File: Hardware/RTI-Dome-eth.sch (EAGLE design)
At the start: 87 parts, among them IC1 24AA128ST, IC3 FT232RL, IC4 REG1117, IC5 74LVC245, IC6 74ABT245, J1 POWERPOLE_POWER45A, U1 W5500, X13 PN61729-S, X9 J1011F21PNL

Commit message: Fix some componenent manufacturer reference
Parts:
- IC6: device rti:74LVC245 -> rti:74ABT245
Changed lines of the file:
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@@
 <part name="X6" library="con-ptr500" deviceset="AK500/6" device=""/>
 <part name="IC5" library="rti" deviceset="74*245" device="" technology="LVC"/>
-<part name="IC6" library="rti" deviceset="74*245" device="" technology="LVC" value="74ABT245"/>
+<part name="IC6" library="rti" deviceset="74*245" device="" technology="ABT" value="74ABT245"/>
 <part name="GND7" library="supply1" deviceset="GND" device=""/>
 <part name="R22" library="rti" deviceset="R-EU" device="'0805'" value="4.7K"/>

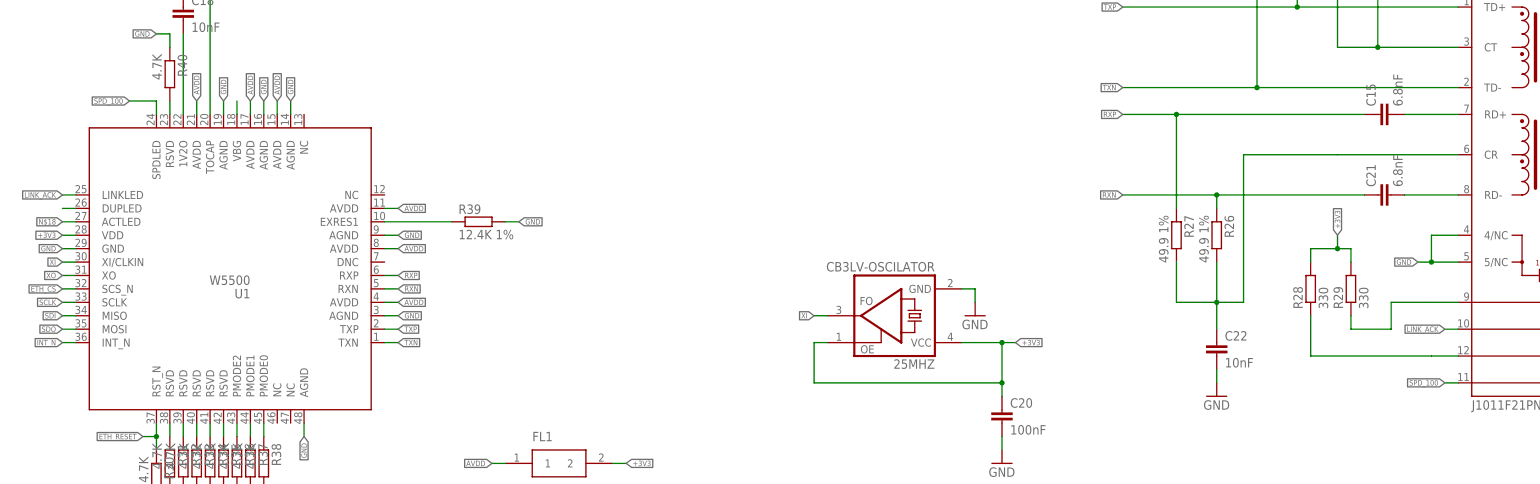
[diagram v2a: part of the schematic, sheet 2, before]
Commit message: Fix ethernet LED.
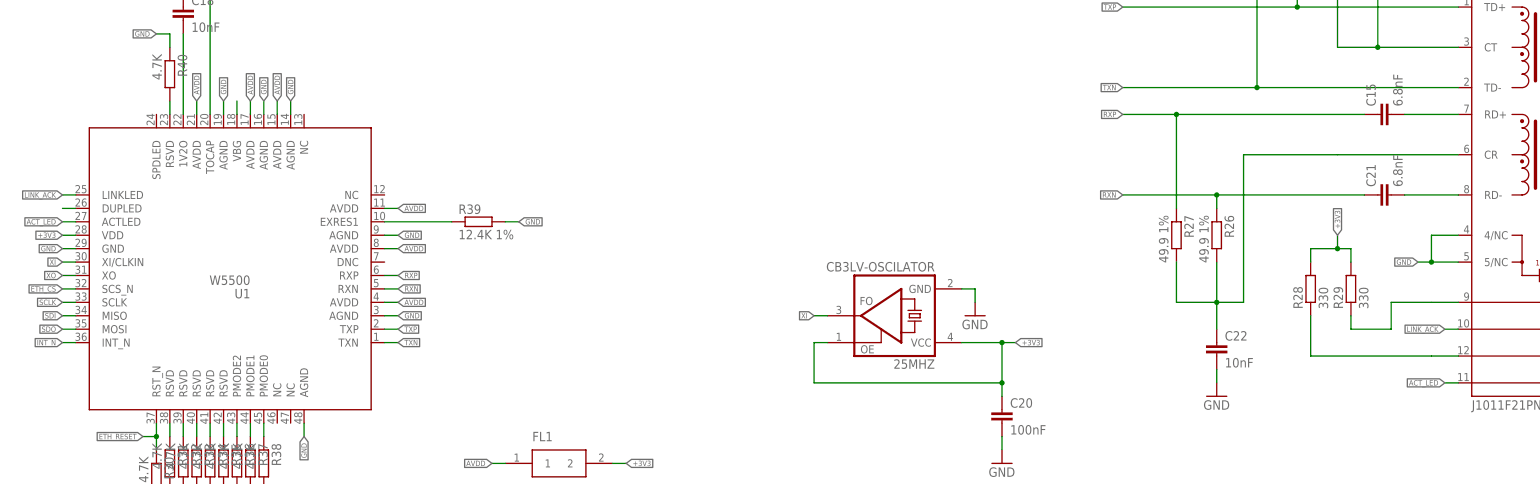
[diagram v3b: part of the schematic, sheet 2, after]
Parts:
- C25, C26: device rti:C-EU'1206' -> rti:C-EU'0805'
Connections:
- removed net N$18: U1.ACTLED
- removed net SPD_100: U1.SPDLED, X9.C-L
- new net ACT_LED: U1.ACTLED, X9.C-L
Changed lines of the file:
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@@
 <part name="+3V1" library="supply1" deviceset="+3V3" device=""/>
 <part name="P+13" library="supply1" deviceset="VCC" device=""/>
-<part name="C25" library="rti" deviceset="C-EU" device="'1206'" value="10uF"/>
-<part name="C26" library="rti" deviceset="C-EU" device="'1206'" value="10uF"/>
+<part name="C25" library="rti" deviceset="C-EU" device="'0805'" value="10uF"/>
+<part name="C26" library="rti" deviceset="C-EU" device="'0805'" value="10uF"/>
 <part name="GND20" library="supply1" deviceset="GND" device=""/>
 <part name="C15" library="rti" deviceset="C-EU" device="'0805'" value="6.8nF"/>
@@
 </segment>
 </net>
-<net name="SPD_100" class="0">
-<segment>
-<pinref part="X9" gate="G$1" pin="C-L"/>
-<wire x1="307.34" y1="149.86" x2="309.88" y2="149.86" width="0.1524" layer="91"/>
-<label x="307.34" y="149.86" size="1.016" layer="95" rot="R180" xref="yes"/>
-</segment>
-<segment>
-<pinref part="U1" gate="G$1" pin="SPDLED"/>
-<wire x1="63.5" y1="203.2" x2="63.5" y2="200.66" width="0.1524" layer="91"/>
-<wire x1="63.5" y1="203.2" x2="58.42" y2="203.2" width="0.1524" layer="91"/>
-<label x="58.42" y="203.2" size="1.016" layer="95" rot="R180" xref="yes"/>
-</segment>
-</net>
 <net name="LINK_ACK" class="0">
 <segment>
@@
 </segment>
 </net>
-<net name="N$18" class="0">
+<net name="ACT_LED" class="0">
 <segment>
 <pinref part="U1" gate="G$1" pin="ACTLED"/>
@@
 <label x="45.72" y="180.34" size="1.016" layer="95" rot="R180" xref="yes"/>
 </segment>
-</net>
+<segment>
+<pinref part="X9" gate="G$1" pin="C-L"/>
+<wire x1="307.34" y1="149.86" x2="309.88" y2="149.86" width="0.1524" layer="91"/>
+<label x="307.34" y="149.86" size="1.016" layer="95" rot="R180" xref="yes"/>
+</segment>
+</net>

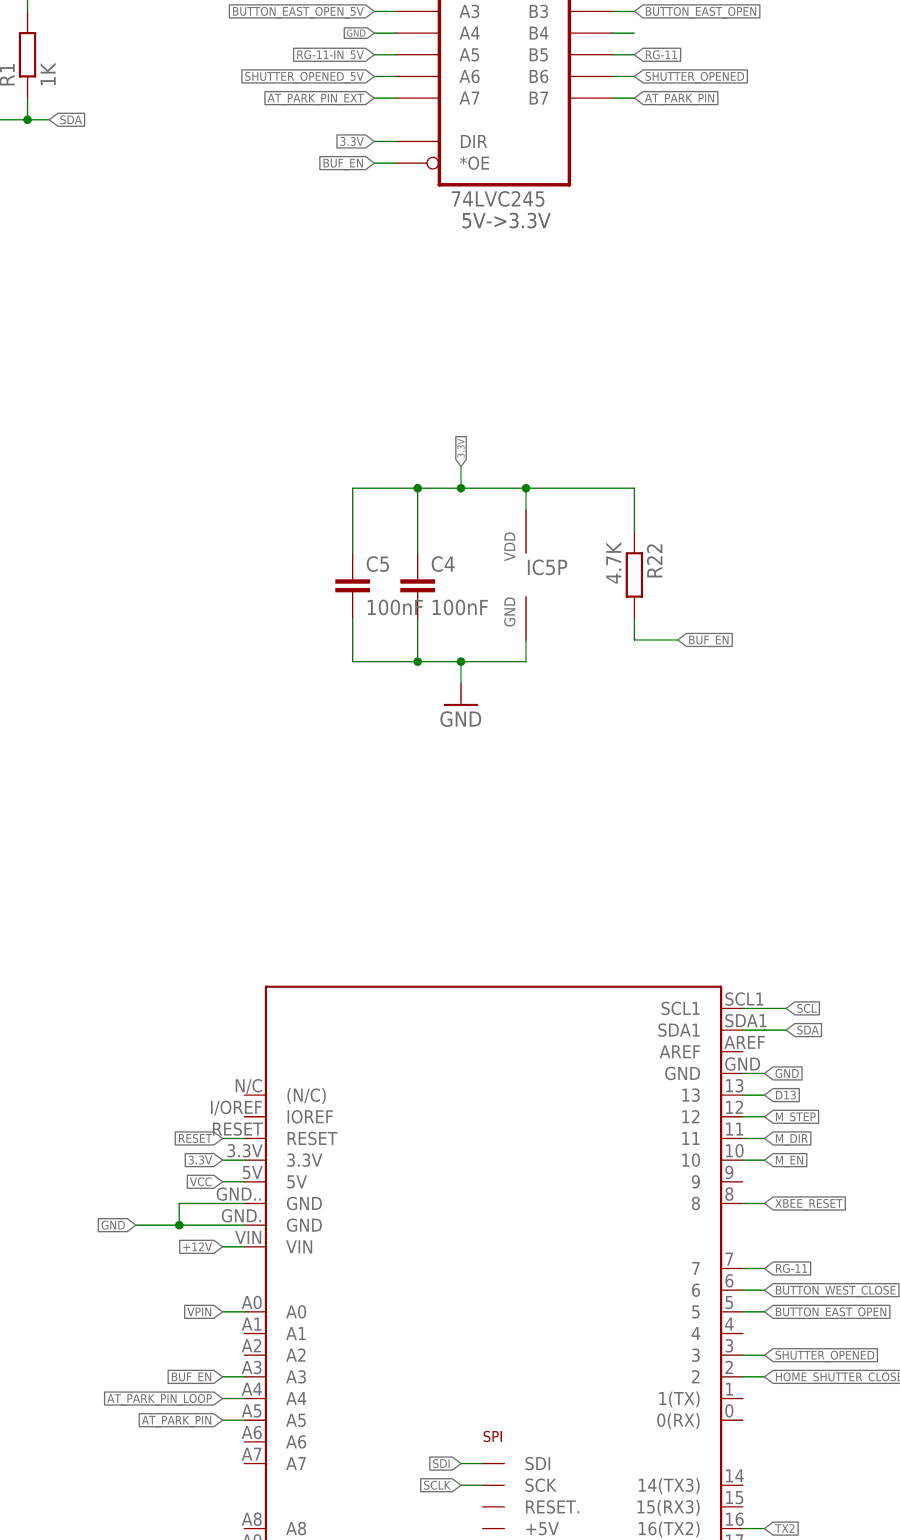
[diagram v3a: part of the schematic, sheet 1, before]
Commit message: Trace optimisation around the FTDI chip
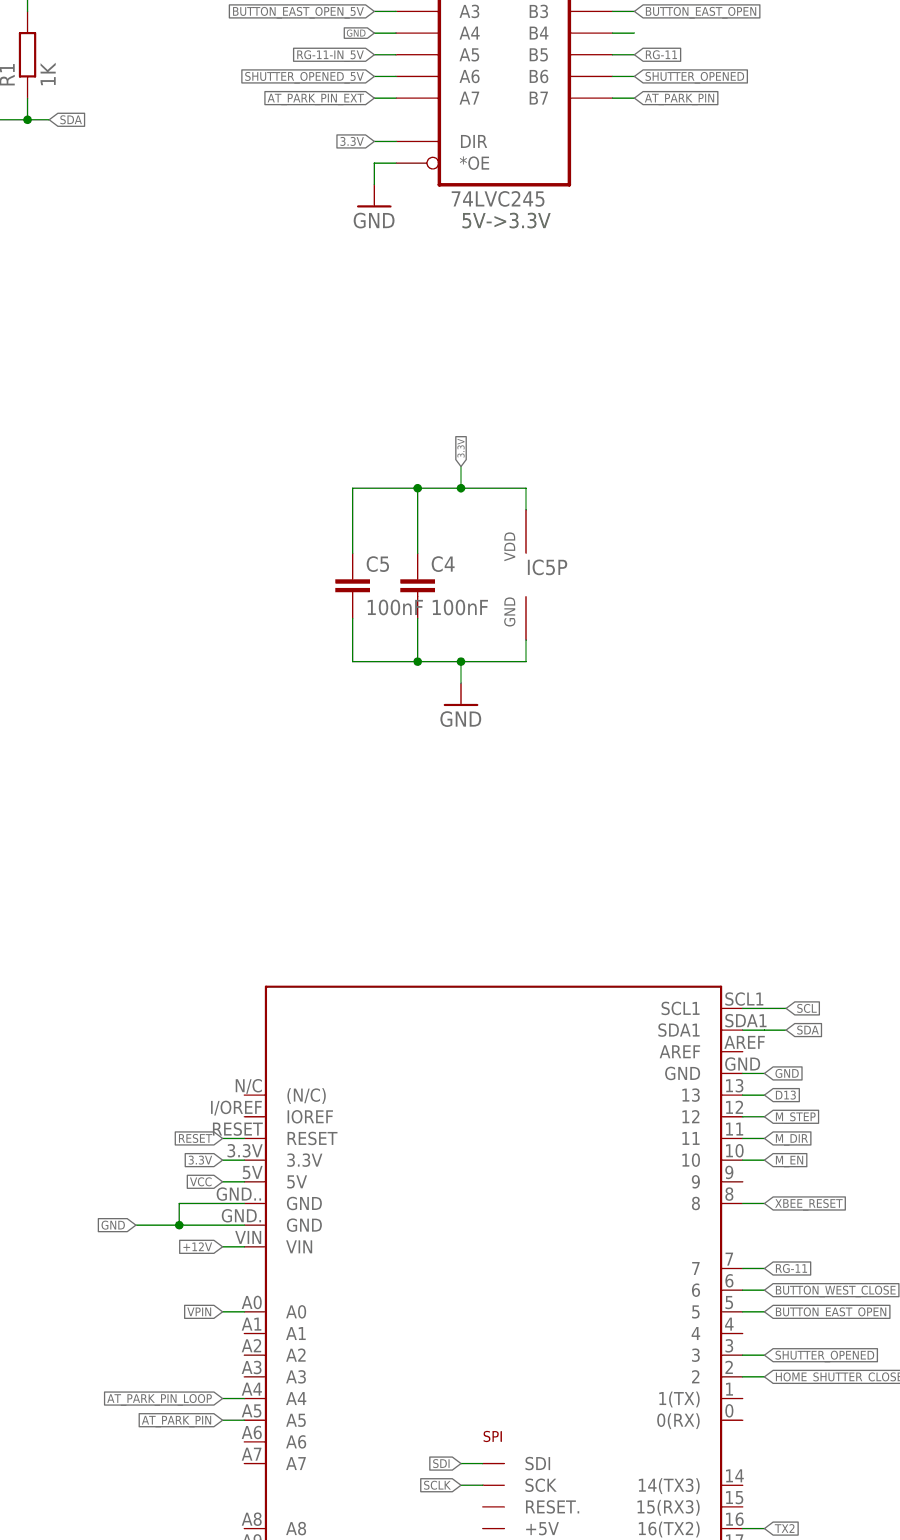
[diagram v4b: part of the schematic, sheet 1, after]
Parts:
- removed R22: 4.7K, rti:R-EU'0805'
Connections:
- removed net BUF_EN: IC5G$1.*OE, R22.2, U$1.A3
- net +12V: now also C25.1, IC4.VIN
- net 3.3V: no longer R22.1
- net GND: now also IC5G$1.*OE
- net VCC: no longer C25.1, IC4.VIN
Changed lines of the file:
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@@
 <part name="IC6" library="rti" deviceset="74*245" device="" technology="ABT" value="74ABT245"/>
 <part name="GND7" library="supply1" deviceset="GND" device=""/>
-<part name="R22" library="rti" deviceset="R-EU" device="'0805'" value="4.7K"/>
 <part name="U$1" library="arduino_shield" deviceset="ARDUINO_DUE_SHIELD_FULL" device=""/>
 <part name="GND9" library="supply1" deviceset="GND" device=""/>
@@
 <part name="IC4" library="burr-brown" deviceset="REG1117" device=""/>
 <part name="+3V1" library="supply1" deviceset="+3V3" device=""/>
-<part name="P+13" library="supply1" deviceset="VCC" device=""/>
 <part name="C25" library="rti" deviceset="C-EU" device="'0805'" value="10uF"/>
 <part name="C26" library="rti" deviceset="C-EU" device="'0805'" value="10uF"/>
@@
 <part name="GND19" library="supply1" deviceset="GND" device=""/>
 <part name="FRAME2" library="frames" deviceset="DINA3_L" device=""/>
+<part name="GND16" library="supply1" deviceset="GND" device=""/>
 </parts>
 <sheets>
@@
 <instance part="IC6" gate="P" x="203.2" y="180.34" rot="R270"/>
 <instance part="GND7" gate="1" x="187.96" y="226.06"/>
-<instance part="R22" gate="G$1" x="147.32" y="180.34" rot="R270"/>
 <instance part="U$1" gate="G$1" x="132.08" y="86.36"/>
 <instance part="GND9" gate="1" x="109.22" y="10.16"/>
@@
 <instance part="U$2" gate="G$1" x="53.34" y="63.5"/>
 <instance part="GND18" gate="1" x="38.1" y="55.88"/>
+<instance part="GND16" gate="1" x="116.84" y="223.52"/>
 </instances>
 <busses>
@@
 <pinref part="GND18" gate="1" pin="GND"/>
 </segment>
+<segment>
+<pinref part="IC5" gate="G$1" pin="*OE"/>
+<wire x1="119.38" y1="228.6" x2="116.84" y2="228.6" width="0.1524" layer="91"/>
+<wire x1="116.84" y1="228.6" x2="116.84" y2="226.06" width="0.1524" layer="91"/>
+<pinref part="GND16" gate="1" pin="GND"/>
+</segment>
 </net>
 <net name="+12V" class="1">
@@
 <junction x="121.92" y="190.5"/>
 <pinref part="IC5" gate="P" pin="VDD"/>
-<pinref part="R22" gate="G$1" pin="1"/>
-<wire x1="134.62" y1="190.5" x2="147.32" y2="190.5" width="0.1524" layer="91"/>
-<wire x1="147.32" y1="190.5" x2="147.32" y2="185.42" width="0.1524" layer="91"/>
-<junction x="134.62" y="190.5"/>
 </segment>
 <segment>
@@
 <wire x1="307.34" y1="160.02" x2="307.34" y2="157.48" width="0.1524" layer="91"/>
 <junction x="307.34" y="160.02"/>
-</segment>
-</net>
-<net name="BUF_EN" class="0">
-<segment>
-<pinref part="IC5" gate="G$1" pin="*OE"/>
-<wire x1="116.84" y1="228.6" x2="119.38" y2="228.6" width="0.1524" layer="91"/>
-<label x="116.84" y="228.6" size="1.016" layer="95" rot="R180" xref="yes"/>
-</segment>
-<segment>
-<pinref part="R22" gate="G$1" pin="2"/>
-<wire x1="152.4" y1="172.72" x2="147.32" y2="172.72" width="0.1524" layer="91"/>
-<wire x1="147.32" y1="172.72" x2="147.32" y2="175.26" width="0.1524" layer="91"/>
-<label x="152.4" y="172.72" size="1.016" layer="95" xref="yes"/>
-</segment>
-<segment>
-<wire x1="99.06" y1="86.36" x2="101.6" y2="86.36" width="0.1524" layer="91"/>
-<label x="99.06" y="86.36" size="1.016" layer="95" rot="R180" xref="yes"/>
-<pinref part="U$1" gate="G$1" pin="A3"/>
 </segment>
 </net>
@@
 <instance part="IC4" gate="G$1" x="58.42" y="27.94"/>
 <instance part="+3V1" gate="G$1" x="73.66" y="35.56"/>
-<instance part="P+13" gate="VCC" x="43.18" y="35.56"/>
 <instance part="C25" gate="G$1" x="43.18" y="20.32"/>
 <instance part="C26" gate="G$1" x="73.66" y="20.32"/>
@@
 </segment>
 </net>
-<net name="VCC" class="0">
-<segment>
-<wire x1="43.18" y1="33.02" x2="43.18" y2="27.94" width="0.1524" layer="91"/>
-<pinref part="IC4" gate="G$1" pin="VIN"/>
-<wire x1="43.18" y1="27.94" x2="45.72" y2="27.94" width="0.1524" layer="91"/>
-<pinref part="P+13" gate="VCC" pin="VCC"/>
-<pinref part="C25" gate="G$1" pin="1"/>
-<wire x1="43.18" y1="22.86" x2="43.18" y2="27.94" width="0.1524" layer="91"/>
-<junction x="43.18" y="27.94"/>
-</segment>
-</net>
 <net name="SDI" class="0">
 <segment>
@@
 </segment>
 </net>
+<net name="+12V" class="1">
+<segment>
+<pinref part="C25" gate="G$1" pin="1"/>
+<pinref part="IC4" gate="G$1" pin="VIN"/>
+<wire x1="43.18" y1="22.86" x2="43.18" y2="27.94" width="0.1524" layer="91"/>
+<wire x1="43.18" y1="27.94" x2="45.72" y2="27.94" width="0.1524" layer="91"/>
+<wire x1="43.18" y1="30.48" x2="43.18" y2="27.94" width="0.1524" layer="91"/>
+<junction x="43.18" y="27.94"/>
+<label x="43.18" y="30.48" size="1.016" layer="95" rot="R90" xref="yes"/>
+</segment>
+</net>

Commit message: Fix dimention layer on  RTI-Dome-eth.brd, added MPN on all component for mouser.
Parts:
- 25MHZ: MPN (none) -> CB3LV-3I-25M0000
- C1, C25, C26, C3: MPN (none) -> CC0805KKX5R8BB106
- C10: MPN (none) -> CC0805JRX7R8BB223
- C11, C12, C14, C16, C17, C20, C4, C5, C6, C7, C8, C9: MPN (none) -> 0805YD104KAT2A
- C13, C18, C22: MPN (none) -> CC0805KRX7R9BB103
- C15, C21: MPN (none) -> C0805C682F4HACTU
- C19: MPN (none) -> C0805C475J3RACTU
- C2: MPN (none) -> MAL215099804E3
- FL1: MPN (none) -> BLM21AG121SN1D
- IC3: MPN (none) -> FT232RL-REEL
- IC4: MPN (none) -> REG1117-3.3/2K5
- IC5: MPN (none) -> 74LVC245APW,112
- IC6: MPN (none) -> 74ABT245PW,112
- R1, R3: MPN (none) -> RT0805FRE071KL
- R10, R2, R6, R7, R8: MPN (none) -> AT0805BRD07100KL
- R11: MPN (none) -> RT0805FRE0710KL
- R12, R13, R14, R15, R16, R17, R18, R19, R20, R21, R30, R31, R32, R33, R34, R35, R36, R37, R38, R4, R40, R9: MPN (none) -> RT0805FRE074K7L
- R23: MPN (none) -> RT0805FRE1310RL
- R24, R25, R26, R27: MPN (none) -> RC0805FR-0749R9L
- R28, R29: MPN (none) -> RC0805JR-07330RL
- R39: MPN (none) -> RC0805FR-0712K4L
- R5: MPN (none) -> RT0805FRD07100RL
- U$2: MPN (none) -> MCP120T-270I/TT
- U1: MPN (none) -> W5500
- X1, X11, X3, X8: MPN (none) -> 691101710002
- X13: MPN (none) -> SS-52300-001
- X4, X5, X7: MPN (none) -> 691101710003
- X6: MPN (none) -> 30.706
- X9: MPN (none) -> J1011F21PNL

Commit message: Cleanup unused boards and sketches
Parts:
- U$2: value MCP120T-270I_TT -> MCP120T-315_TT; device MCP120T-270I_TT:MCP120T-270I_TT -> MCP120T:MCP120T; MPN MCP120T-270I/TT -> MCP120T-315I/TT
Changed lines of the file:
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@@
 <attribute name="MPN" value="RT0805FRE074K7L"/>
 </part>
-<part name="U$2" library="MCP120T-270I_TT" deviceset="MCP120T-270I_TT" device="">
-<attribute name="MPN" value="MCP120T-270I/TT"/>
+<part name="U$2" library="MCP120T" deviceset="MCP120T" device="" value="MCP120T-315_TT">
+<attribute name="MPN" value="MCP120T-315I/TT"/>
 </part>
 <part name="GND18" library="supply1" deviceset="GND" device=""/>
